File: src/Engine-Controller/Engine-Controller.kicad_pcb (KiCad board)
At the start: 4 copper layers, 101.6 x 50.8 mm, 48 parts, among them J1 Jumper_NO, P1 EJ508A, P2 USB, P3 SBH11-PBPC-D05-RA-BK, P4 0901471110, P5 66953-005LF, P6 Micro_SD_Card, P7 0901471110, U1 STM32L443VCT6, U2 LM22672MRE-5.0_NOPB, U3 LMS8117AMP-3.3_NOPB, U4 SN74LV07ADR, U5 SST25VF040B-50-4I-S2AE-T

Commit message: Added in Micro 3D model to step file
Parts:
- U1: value STM32L443VCT6 -> LQFP100-14x14mm
- U2: value LM22672MRE-5.0_NOPB -> VREG_LM5017MR/NOPB

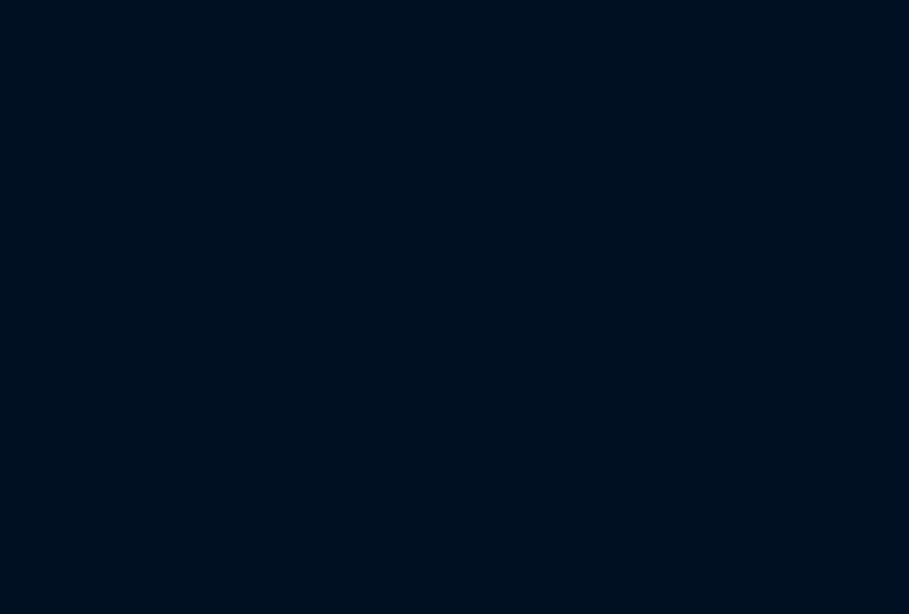
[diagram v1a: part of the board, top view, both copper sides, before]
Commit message: Added new components to PCB
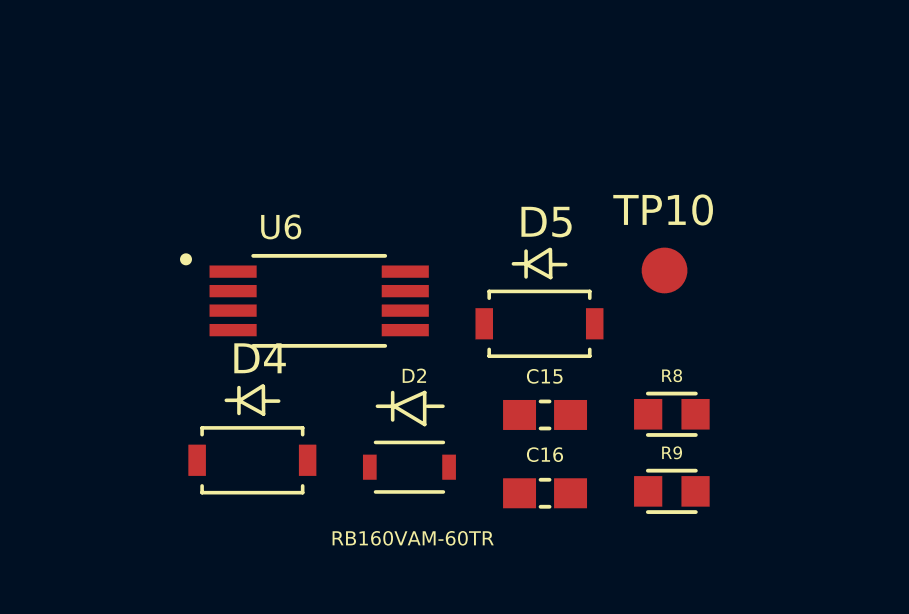
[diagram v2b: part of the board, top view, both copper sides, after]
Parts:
- added C15: 0.1uF, Engine-Controller:CAP_0603, F.Cu at (150.4, 169.1)
- added C16: 0.1uF, Engine-Controller:CAP_0603, F.Cu at (150.4, 171.7)
- added D2: RB160VAM-60TR, Engine-Controller:RB160VAM-60TR, F.Cu at (145.9, 170.8)
- added D4: SM5819PL-TP, Engine-Controller:SM5819PL-TP, F.Cu at (140.6, 170.6)
- added D5: SM5819PL-TP, Engine-Controller:SM5819PL-TP, F.Cu at (150.2, 166.1)
- added R8: 10k, Engine-Controller:RES_0603, F.Cu at (154.6, 169.1)
- added R9: 470, Engine-Controller:RES_0603, F.Cu at (154.6, 171.7)
- added TP10: TP, Engine-Controller:TP, F.Cu at (154.4, 164.3)
- added U6: TPS2115APWR, Engine-Controller:TPS2115APWR, F.Cu at (142.9, 165.3)
- U1: value LQFP100-14x14mm -> STM32L443VCT6
- U2: value VREG_LM5017MR/NOPB -> LM22672MRE-5.0_NOPB
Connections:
- C1 pad 1: VIN -> /power/VIN
- C2 pad 2: VIN -> /power/VIN
- C5 pad 1: 5V -> 5V_BUCK
- C6 pad 1: 5V -> /power/5V
- L1 pad 2: 5V -> 5V_BUCK
- P1 pad 1: VIN -> /power/V_JACK
- P1 pad 3: Net-(P1-Pad3) -> Earth
- P2 pad 1: 5V -> 5V_USB
- P5 pad A1: VIN -> V_HEAD
- R2 pad 2: VIN -> /power/VIN
- R4 pad 2: 5V -> 5V_BUCK
- TP2 pad 1: VIN -> /power/VIN
- TP4 pad 1: 5V -> /power/5V
- U1 pad 4: Net-(U1-Pad4) -> 5V_SRC
- U2 pad 7: VIN -> /power/VIN
- U3 pad 3: 5V -> /power/5V

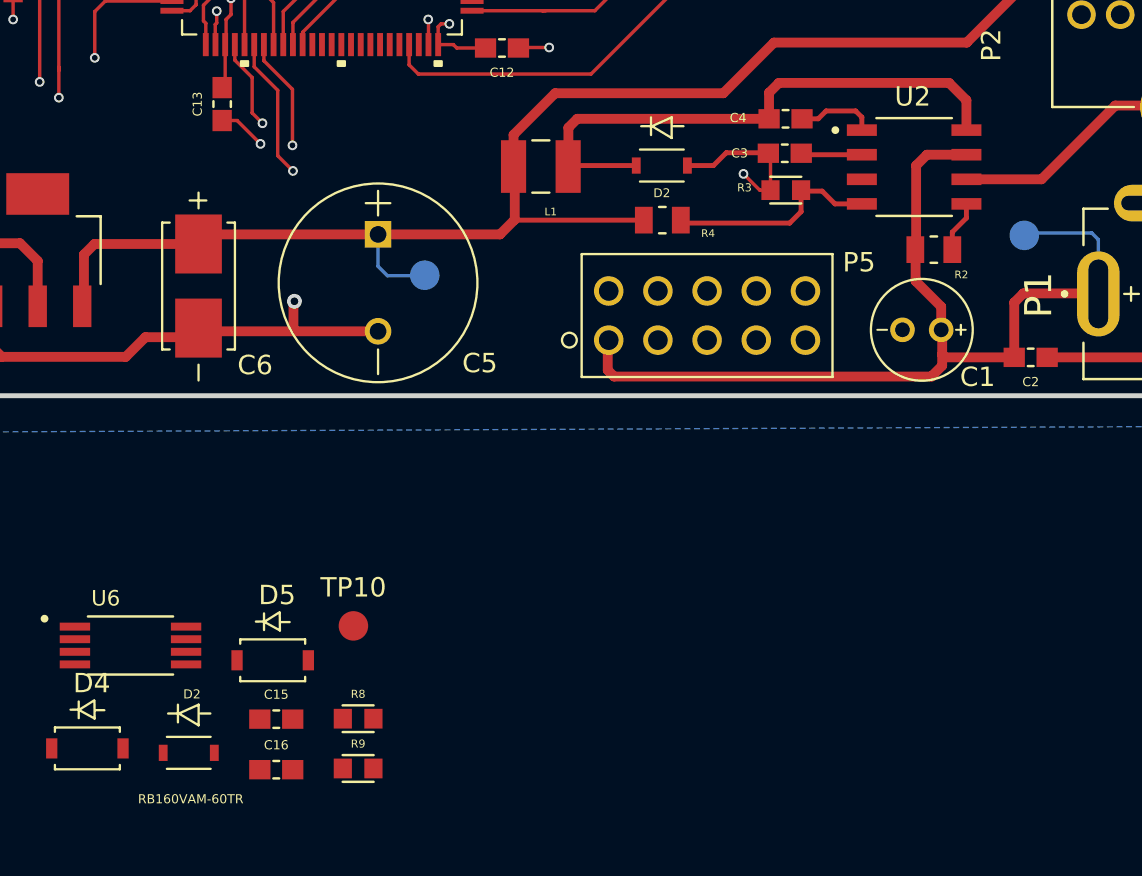
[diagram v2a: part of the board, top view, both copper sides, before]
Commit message: Added new C1 cap to PCB layout
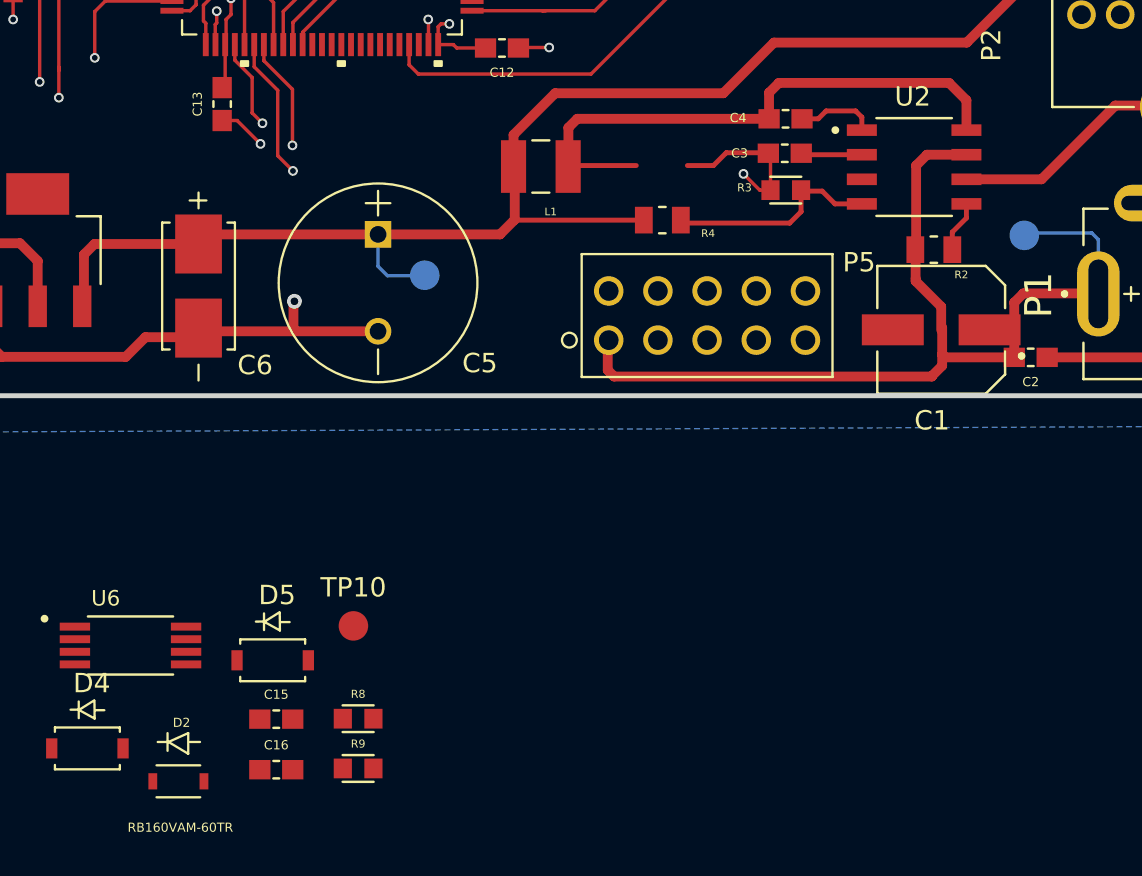
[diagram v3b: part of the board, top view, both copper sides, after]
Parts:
- removed the D2 at (170.3, 140.5)
- C1: value 22uF -> 68uF; footprint Engine-Controller:UKL1C220KDDANATD -> Engine-Controller:EEEFPV680XAP
- moved D2 1.56 mm to (145.3, 172.3)

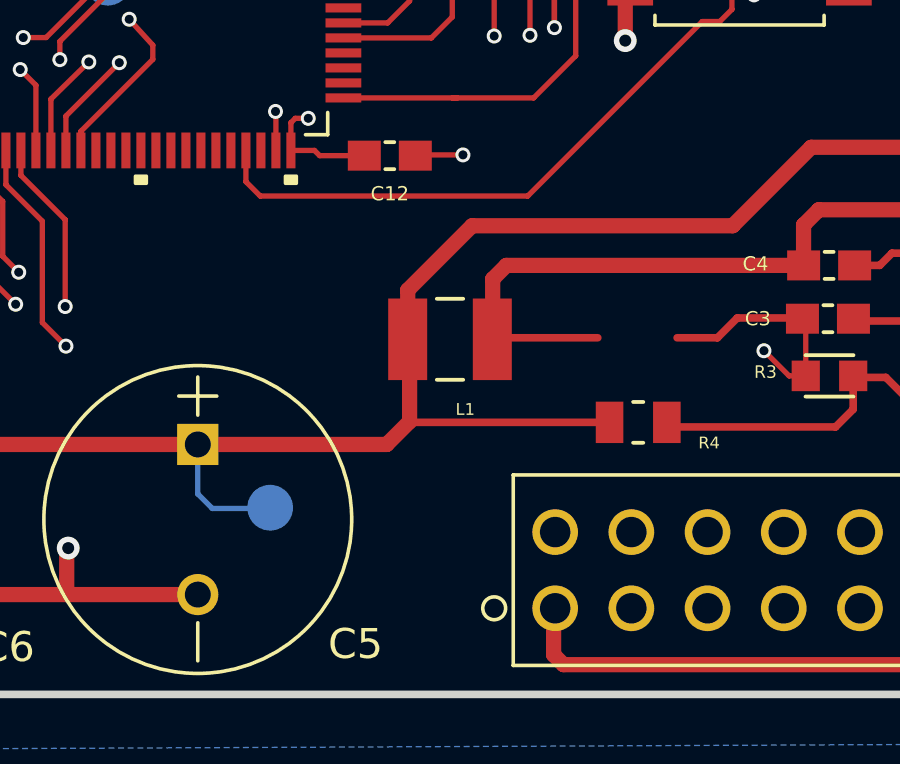
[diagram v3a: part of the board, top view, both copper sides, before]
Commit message: Updated L1 inductor
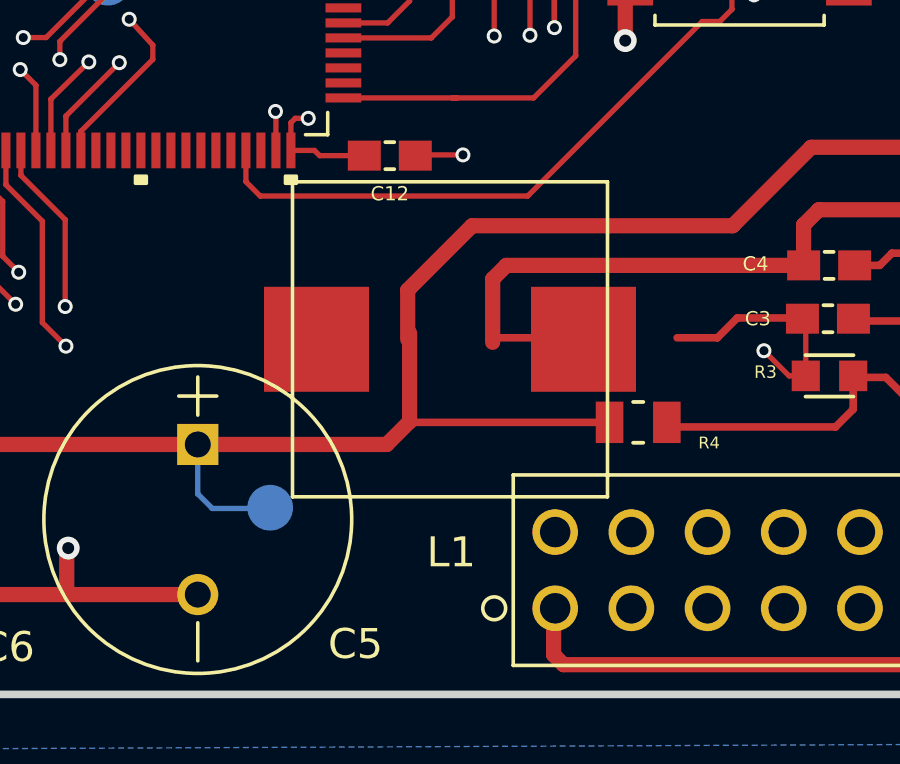
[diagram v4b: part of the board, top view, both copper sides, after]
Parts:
- L1: value 22uH -> 33uH; footprint Engine-Controller:CBC3225T220KR -> Engine-Controller:SRP1038A-330M

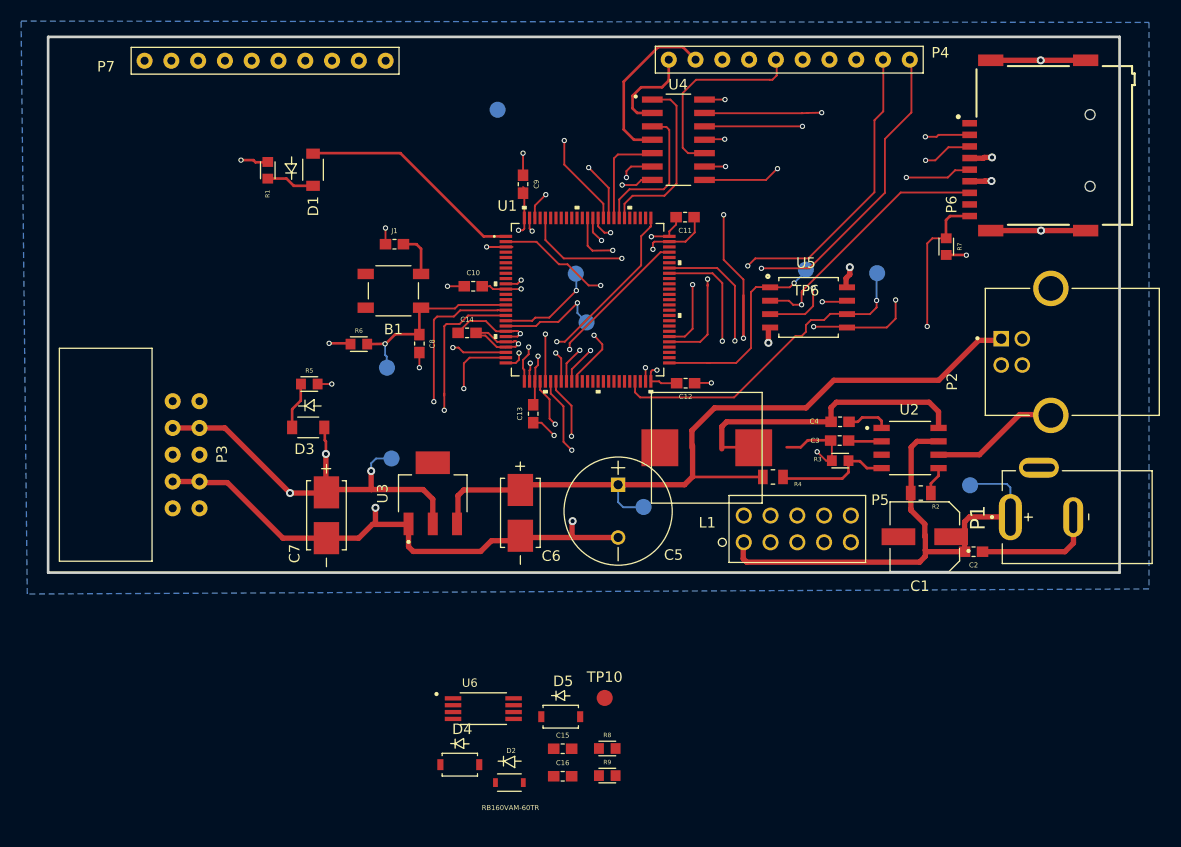
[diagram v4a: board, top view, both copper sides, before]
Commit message: Removed SWD 3.3V connections
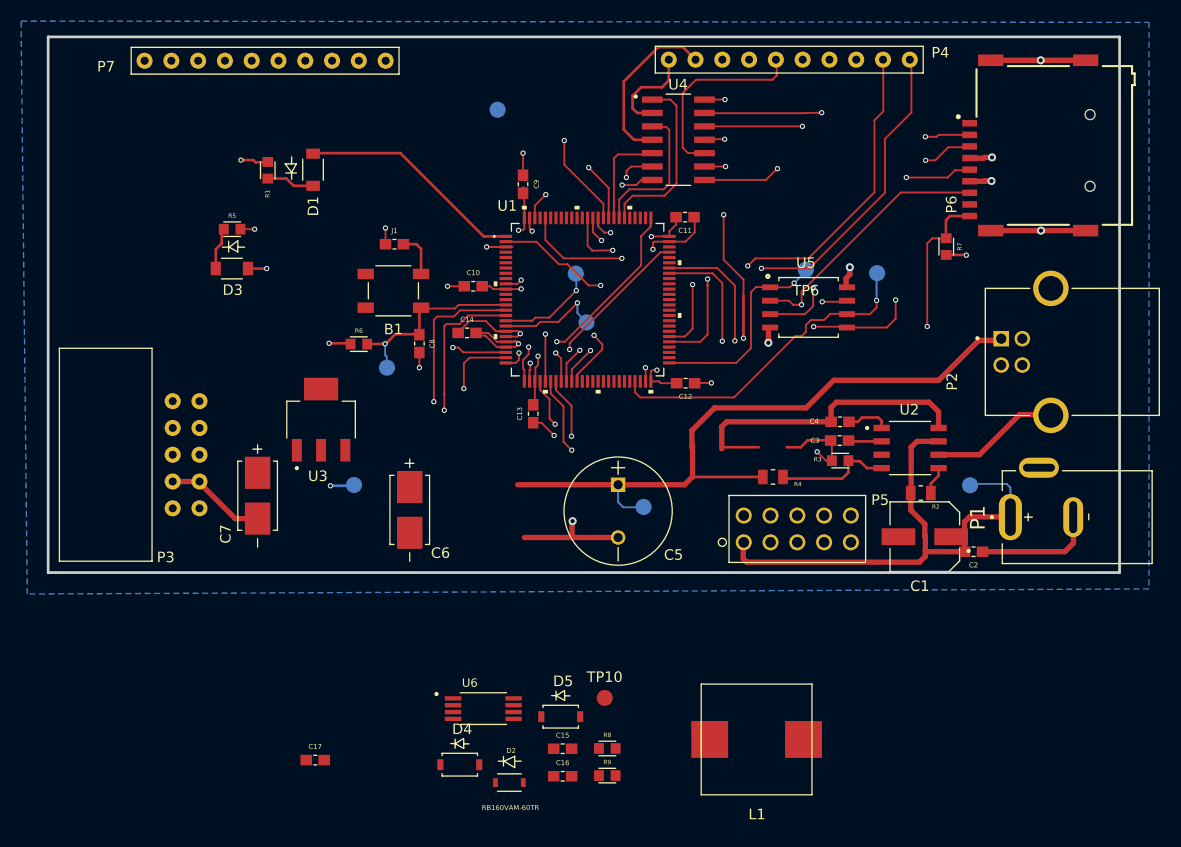
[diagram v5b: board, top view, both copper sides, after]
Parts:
- added C17: 1uF, Engine-Controller:CAP_0603, F.Cu at (126.9, 170.2)
- moved L1 28.1 mm to (168.8, 168.2)
- moved D3 16.7 mm to (119.0, 123.6)
- moved R5 16.4 mm to (119.0, 119.8)
- moved U3 12.7 mm to (127.5, 137.9)
- moved C6 10.5 mm to (135.9, 146.5)
- moved C7 6.79 mm to (121.5, 145.1)
- moved TP5 4.36 mm to (130.6, 144.1)
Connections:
- P3 pad A2: 3.3V -> Net-(P3-PadA2)
- P3 pad B2: 3.3V -> Net-(P3-PadB2)
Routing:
- net 3.3V: track 81.2 -> 44.2 mm, vias 14 -> 13
- net Earth: track 143.4 -> 112.5 mm, vias 22 -> 21
- net 5V: track 74.5 -> 65.4 mm

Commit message: Finished Routing Rev 2 changes
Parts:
- TP10: moved to B.Cu
- moved D4 47.1 mm to (182.6, 149.1), turned to 270 degrees
- moved R9 43.1 mm to (128.9, 137.1)
- moved D5 42.0 mm to (188.7, 149.3), turned to 270 degrees
- moved R8 35.8 mm to (133.5, 140.2)
- moved TP10 34.6 mm to (133.3, 136.9)
- moved C17 32.1 mm to (137.6, 139.9)
- moved C16 31.2 mm to (128.6, 149.4), turned to 90 degrees
- moved D2 29.2 mm to (161.4, 148.0), turned to 270 degrees
- moved L1 29.0 mm to (149.9, 146.3), turned to 0 degrees
- moved C15 27.7 mm to (131.0, 149.4), turned to 90 degrees
- moved TP4 26.0 mm to (132.2, 144.2)
- moved U6 25.7 mm to (129.8, 143.2), turned to 270 degrees
- moved C5 18.7 mm to (137.6, 149.0), turned to 90 degrees
- moved C2 14.7 mm to (180.9, 138.5), turned to 90 degrees
- moved C6 13.2 mm to (122.9, 149.0), turned to 180 degrees
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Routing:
- net 5V_USB: track 0.00 -> 81.1 mm, vias 0 -> 2
- net 5V: track 65.4 -> 0.00 mm
- net 5V_BUCK: track 0.00 -> 52.9 mm
- net VIN: track 51.9 -> 0.00 mm
- net 5V_SRC: track 0.00 -> 40.4 mm, vias 0 -> 1
- net /power/VIN: track 0.00 -> 35.4 mm, vias 0 -> 1
- net Earth: track 112.5 -> 133.6 mm, vias 21 -> 23
- net /power/5V: track 0.00 -> 16.3 mm, vias 0 -> 1
- net V_HEAD: track 0.00 -> 15.8 mm
- net 3.3V: track 44.2 -> 58.8 mm, vias 13 -> 14
- net Net-(C4-Pad1): track 29.9 -> 38.2 mm
- net /power/V_JACK: track 0.00 -> 8.12 mm
- net Net-(R3-Pad1): track 10.9 -> 5.73 mm
- net Net-(R9-Pad1): track 0.00 -> 3.87 mm
- net Net-(C4-Pad2): track 4.06 -> 3.22 mm
